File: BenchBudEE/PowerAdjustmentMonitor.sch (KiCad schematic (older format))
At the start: 0 parts

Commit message: Populated the Power Adjustment Monitor sheet in rough form.
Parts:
- added JP? (x3): JUMPER, ~, symbol JUMPER
- added R? (x8): R, ~, symbol R
- added R? (x2): RVAR, ~, symbol RVAR
- added U? (x2): LM317, ~, symbol LM317
- added U? (x2): 7805, ~, symbol 7805
- added U? (x2): LM324, symbol LM324
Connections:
- net labels added: +12V, +3.3V, +5V, -12V, 3V3_MON, 5V_MON, AGND, FE_V+, FE_V-, GND, V+_ADJ, V+_ADJ_MON, V+_CURR_MON, V+_MON, V-_ADJ, V-_ADJ_MON, V-_CURR_MON, V-_MON
- wire segments 0 -> 77
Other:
- note added: "Jumper to split the nets"
- note added: "Placeholder for now."
- note added: "Placeholder.\nRegulator TBD."

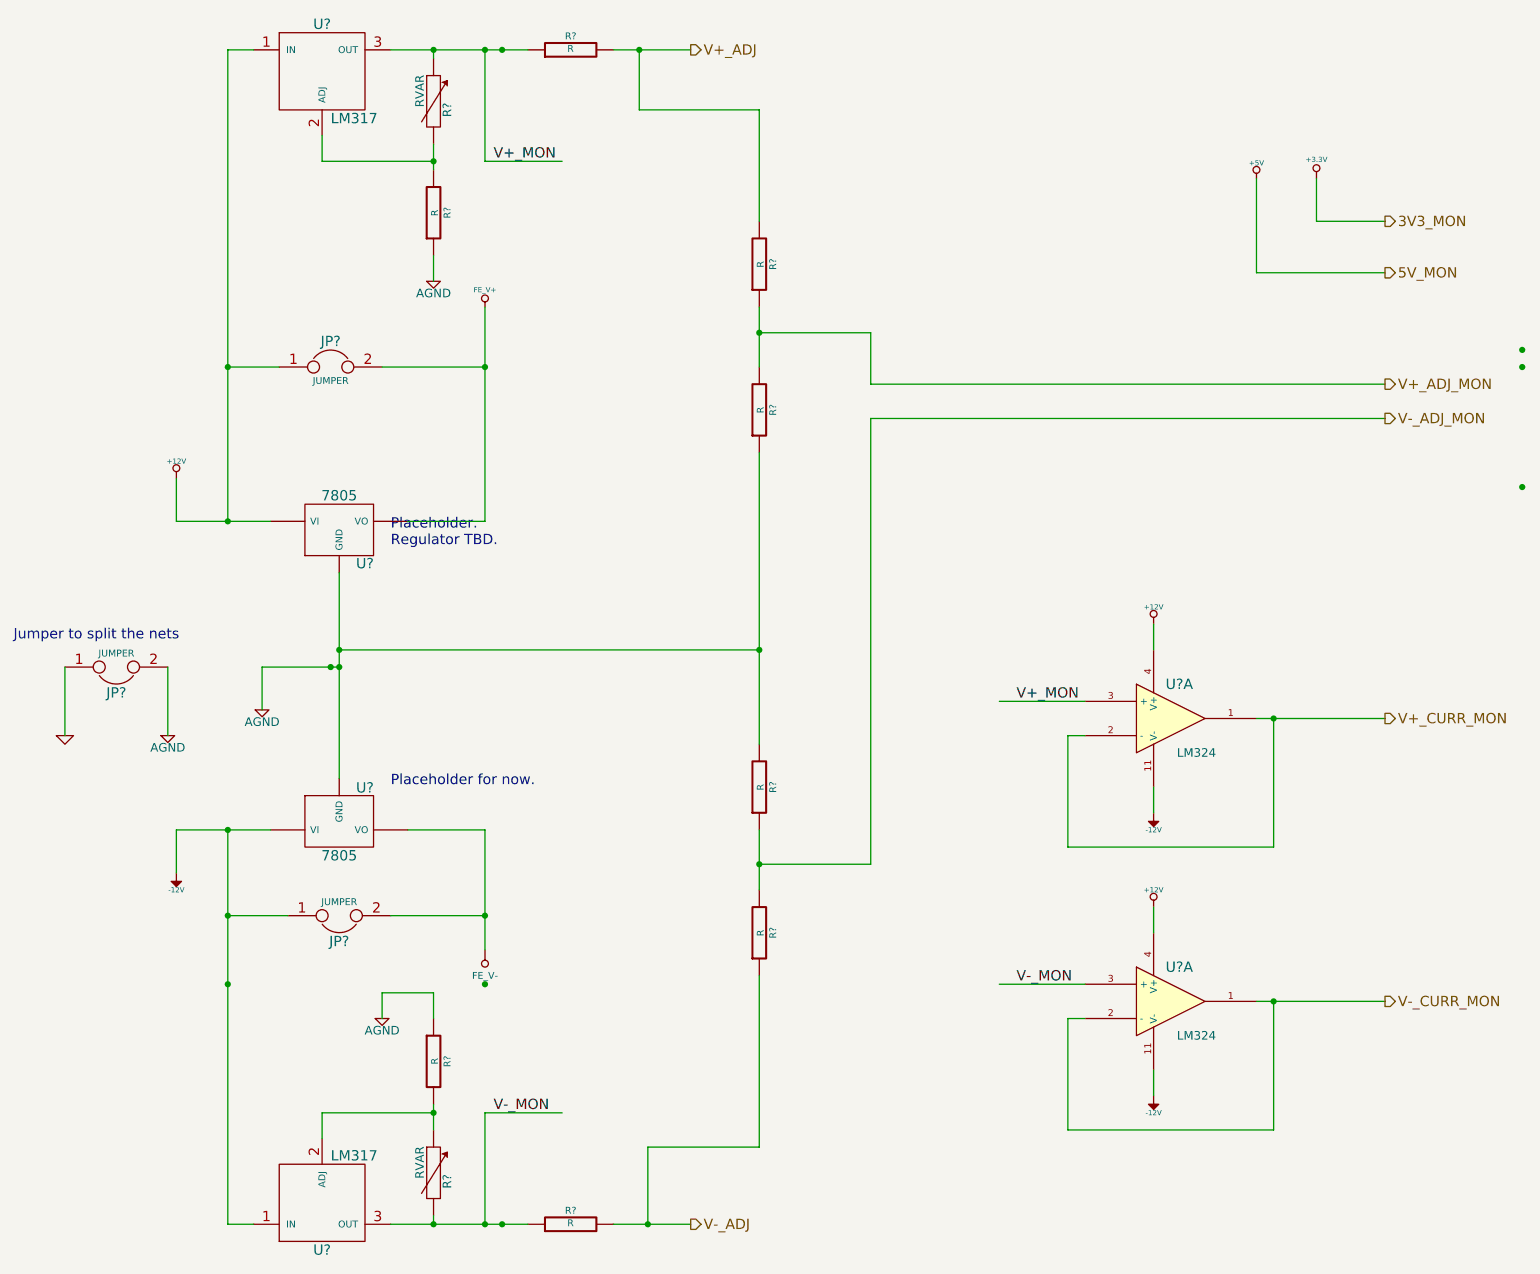
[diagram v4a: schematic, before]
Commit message: Connected Arduino power/ground. +5V power filtering. Removed current monitoring.
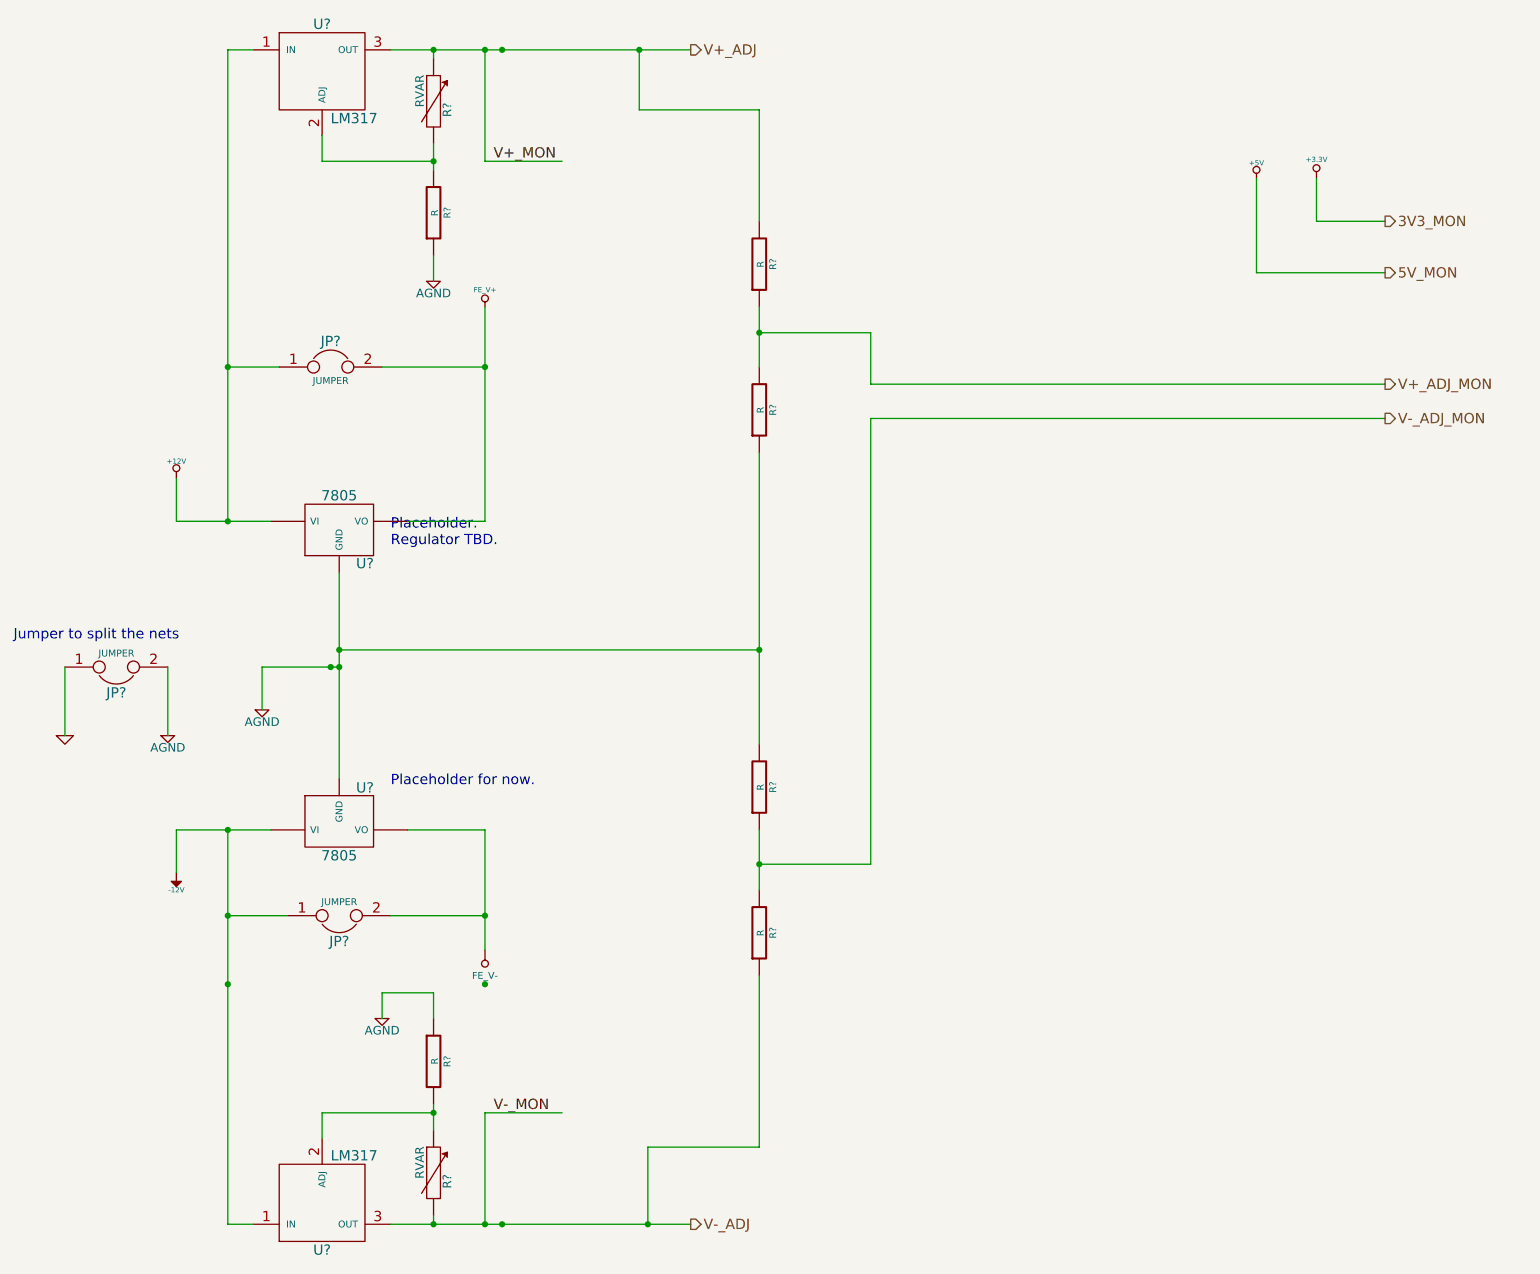
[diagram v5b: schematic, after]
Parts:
- removed R? (x2): R, ~, symbol R
- removed U? (x2): LM324, symbol LM324
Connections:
- net labels removed: V+_CURR_MON, V-_CURR_MON
- wire segments 77 -> 59
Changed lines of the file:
@@
 $Descr A4 11693 8268
 encoding utf-8
-Sheet 9 9
+Sheet 6 9
 Title ""
-Date "14 feb 2014"
+Date "19 feb 2014"
 Rev ""
 Comp ""
@@
 	1    0    0    1
 $EndComp
-Connection ~ 9300 2600
-Connection ~ 9300 2500
-Connection ~ 9300 3300
 Wire Wire Line
 	1450 5550 1450 5300
@@
 Connection ~ 1750 5800
 Wire Wire Line
-	2700 7600 3500 7600
+	2700 7600 4450 7600
 Wire Wire Line
 	2950 7600 2950 7550
@@
 Text HLabel 8500 2900 2    60   Output ~ 0
 V-_ADJ_MON
-Text HLabel 8500 6300 2    60   Output ~ 0
-V-_CURR_MON
-Text HLabel 8500 4650 2    60   Output ~ 0
-V+_CURR_MON
 $Comp
 L R R?
@@
 Wire Wire Line
 	7750 2050 7750 1500
-$Comp
-L R R?
-U 1 1 52F7546A
-P 3750 7600
-F 0 "R?" V 3830 7600 40  0000 C CNN
-F 1 "R" V 3757 7601 40  0000 C CNN
-F 2 "~" V 3680 7600 30  0000 C CNN
-F 3 "~" H 3750 7600 30  0000 C CNN
-	1    3750 7600
-	0    -1   -1   0
-$EndComp
-Wire Wire Line
-	4000 7600 4450 7600
 Wire Wire Line
 	4200 7600 4200 7150
@@
 	4200 7150 4850 7150
 Connection ~ 4200 7600
-$Comp
-L R R?
-U 1 1 52F7576B
-P 3750 750
-F 0 "R?" V 3830 750 40  0000 C CNN
-F 1 "R" V 3757 751 40  0000 C CNN
-F 2 "~" V 3680 750 30  0000 C CNN
-F 3 "~" H 3750 750 30  0000 C CNN
-	1    3750 750
-	0    -1   -1   0
-$EndComp
-Wire Wire Line
-	2700 750  3500 750
-Wire Wire Line
-	4000 750  4450 750
+Wire Wire Line
+	2700 750  4450 750
 Wire Wire Line
 	4850 1100 4150 1100
@@
 Text Label 3300 1400 0    60   ~ 0
 V+_MON
-$Comp
-L LM324 U?
-U 1 1 52F76215
-P 7250 6300
-F 0 "U?" H 7300 6500 60  0000 C CNN
-F 1 "LM324" H 7400 6100 50  0000 C CNN
-F 2 "" H 7250 6300 60  0000 C CNN
-F 3 "" H 7250 6300 60  0000 C CNN
-	1    7250 6300
-	1    0    0    -1
-$EndComp
-$Comp
-L +12V #PWR?
-U 1 1 52F76385
-P 7150 5750
-F 0 "#PWR?" H 7150 5700 20  0001 C CNN
-F 1 "+12V" H 7150 5850 30  0000 C CNN
-F 2 "" H 7150 5750 60  0000 C CNN
-F 3 "" H 7150 5750 60  0000 C CNN
-	1    7150 5750
-	1    0    0    -1
-$EndComp
-Wire Wire Line
-	7150 5750 7150 5900
-$Comp
-L -12V #PWR?
-U 1 1 52F763E4
-P 7150 6850
-F 0 "#PWR?" H 7150 6980 20  0001 C CNN
-F 1 "-12V" H 7150 6950 30  0000 C CNN
-F 2 "" H 7150 6850 60  0000 C CNN
-F 3 "" H 7150 6850 60  0000 C CNN
-	1    7150 6850
-	1    0    0    1
-$EndComp
-Wire Wire Line
-	7150 6850 7150 6700
 Wire Wire Line
 	4850 5500 5500 5500
@@
 	5500 2400 5500 2700
 $Comp
-L LM324 U?
-U 1 1 52F76762
-P 7250 4650
-F 0 "U?" H 7300 4850 60  0000 C CNN
-F 1 "LM324" H 7400 4450 50  0000 C CNN
-F 2 "" H 7250 4650 60  0000 C CNN
-F 3 "" H 7250 4650 60  0000 C CNN
-	1    7250 4650
-	1    0    0    -1
-$EndComp
-$Comp
-L +12V #PWR?
-U 1 1 52F76768
-P 7150 4100
-F 0 "#PWR?" H 7150 4050 20  0001 C CNN
-F 1 "+12V" H 7150 4200 30  0000 C CNN
-F 2 "" H 7150 4100 60  0000 C CNN
-F 3 "" H 7150 4100 60  0000 C CNN
-	1    7150 4100
-	1    0    0    -1
-$EndComp
-Wire Wire Line
-	7150 4100 7150 4250
-$Comp
-L -12V #PWR?
-U 1 1 52F7676F
-P 7150 5200
-F 0 "#PWR?" H 7150 5330 20  0001 C CNN
-F 1 "-12V" H 7150 5300 30  0000 C CNN
-F 2 "" H 7150 5200 60  0000 C CNN
-F 3 "" H 7150 5200 60  0000 C CNN
-	1    7150 5200
-	1    0    0    1
-$EndComp
-Wire Wire Line
-	7150 5200 7150 5050
-Wire Wire Line
-	8500 6300 7750 6300
-Wire Wire Line
-	8500 4650 7750 4650
-Wire Wire Line
-	6750 4750 6650 4750
-Wire Wire Line
-	6650 4750 6650 5400
-Wire Wire Line
-	6650 5400 7850 5400
-Wire Wire Line
-	7850 5400 7850 4650
-Connection ~ 7850 4650
-Wire Wire Line
-	6750 4550 6250 4550
-Text Label 6350 4550 0    60   ~ 0
-V+_MON
-Wire Wire Line
-	6750 6400 6650 6400
-Wire Wire Line
-	6650 6400 6650 7050
-Wire Wire Line
-	6650 7050 7850 7050
-Wire Wire Line
-	7850 7050 7850 6300
-Connection ~ 7850 6300
-Wire Wire Line
-	6750 6200 6250 6200
-Text Label 6350 6200 0    60   ~ 0
-V-_MON
-$Comp
 L RVAR R?

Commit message: Placed the relay components.
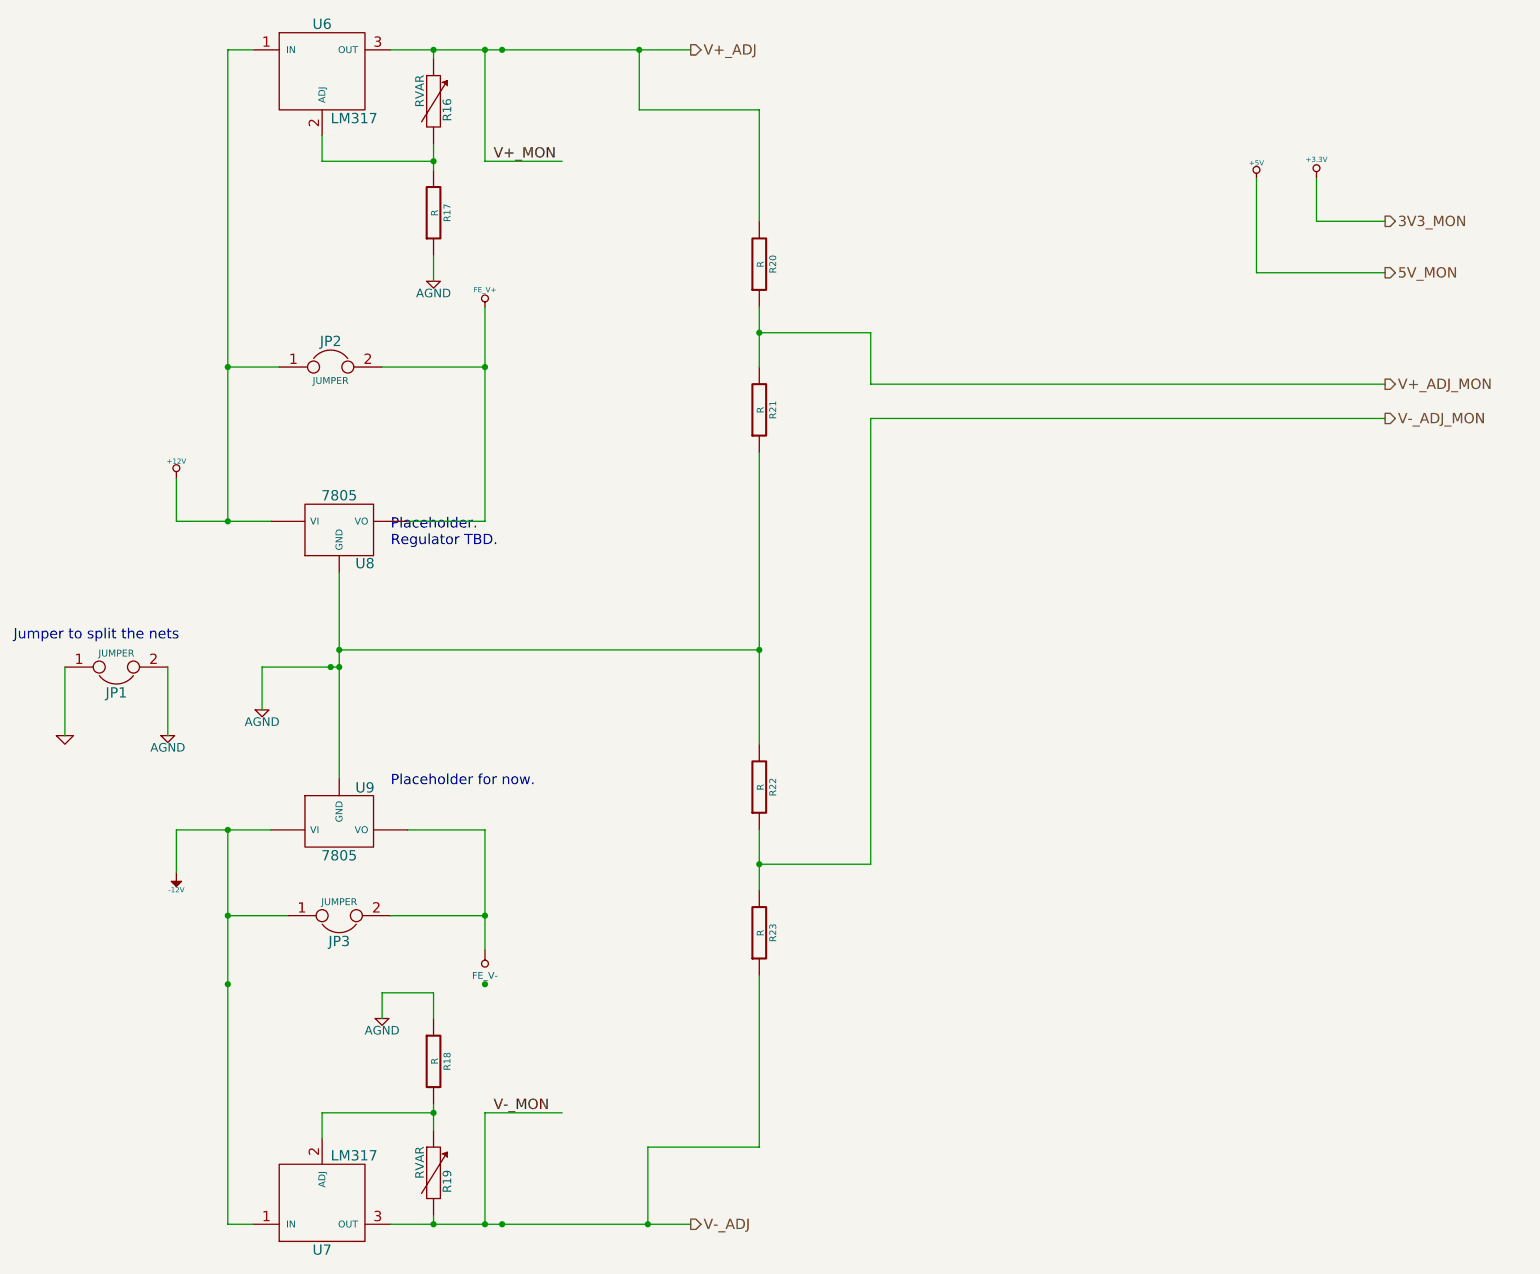
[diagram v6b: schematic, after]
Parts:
- gave numbers to parts that had none: 15
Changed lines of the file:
@@
 Sheet 6 9
 Title ""
-Date "19 feb 2014"
+Date "20 feb 2014"
 Rev ""
 Comp ""
@@
 $EndDescr
 $Comp
-L +12V #PWR?
+L +12V #PWR35
 U 1 1 52F6DADC
 P 1450 3250
-F 0 "#PWR?" H 1450 3200 20  0001 C CNN
+F 0 "#PWR35" H 1450 3200 20  0001 C CNN
 F 1 "+12V" H 1450 3350 30  0000 C CNN
 F 2 "" H 1450 3250 60  0000 C CNN
@@
 $EndComp
 $Comp
-L -12V #PWR?
+L -12V #PWR36
 U 1 1 52F6DAE4
 P 1450 5550
-F 0 "#PWR?" H 1450 5680 20  0001 C CNN
+F 0 "#PWR36" H 1450 5680 20  0001 C CNN
 F 1 "-12V" H 1450 5650 30  0000 C CNN
 F 2 "" H 1450 5550 60  0000 C CNN
@@
 $EndComp
 $Comp
-L +5V #PWR?
+L +5V #PWR42
 U 1 1 52F6DB6E
 P 7750 1500
-F 0 "#PWR?" H 7750 1590 20  0001 C CNN
+F 0 "#PWR42" H 7750 1590 20  0001 C CNN
 F 1 "+5V" H 7750 1590 30  0000 C CNN
 F 2 "" H 7750 1500 60  0000 C CNN
@@
 $EndComp
 $Comp
-L +3.3V #PWR?
+L +3.3V #PWR43
 U 1 1 52F6DB74
 P 8100 1500
-F 0 "#PWR?" H 8100 1460 30  0001 C CNN
+F 0 "#PWR43" H 8100 1460 30  0001 C CNN
 F 1 "+3.3V" H 8100 1610 30  0000 C CNN
 F 2 "" H 8100 1500 60  0000 C CNN
@@
 $EndComp
 $Comp
-L LM317 U?
+L LM317 U7
 U 1 1 52F71F0F
 P 2300 7450
-F 0 "U?" H 2300 7750 60  0000 C CNN
+F 0 "U7" H 2300 7750 60  0000 C CNN
 F 1 "LM317" H 2350 7200 60  0000 L CNN
 F 2 "~" H 2300 7450 60  0000 C CNN
@@
 Placeholder.\nRegulator TBD.
 $Comp
-L JUMPER JP?
+L JUMPER JP2
 U 1 1 52F720F4
 P 2350 2600
-F 0 "JP?" H 2350 2750 60  0000 C CNN
+F 0 "JP2" H 2350 2750 60  0000 C CNN
 F 1 "JUMPER" H 2350 2520 40  0000 C CNN
 F 2 "~" H 2350 2600 60  0000 C CNN
@@
 $EndComp
 $Comp
-L JUMPER JP?
+L JUMPER JP3
 U 1 1 52F72101
 P 2400 5800
-F 0 "JP?" H 2400 5950 60  0000 C CNN
+F 0 "JP3" H 2400 5950 60  0000 C CNN
 F 1 "JUMPER" H 2400 5720 40  0000 C CNN
 F 2 "~" H 2400 5800 60  0000 C CNN
@@
 $EndComp
 $Comp
-L GND #PWR?
+L GND #PWR33
 U 1 1 52F72349
 P 800 4750
-F 0 "#PWR?" H 800 4750 30  0001 C CNN
+F 0 "#PWR33" H 800 4750 30  0001 C CNN
 F 1 "GND" H 800 4680 30  0001 C CNN
 F 2 "" H 800 4750 60  0000 C CNN
@@
 $EndComp
 $Comp
-L AGND #PWR?
+L AGND #PWR34
 U 1 1 52F726D0
 P 1400 4750
-F 0 "#PWR?" H 1400 4750 40  0001 C CNN
+F 0 "#PWR34" H 1400 4750 40  0001 C CNN
 F 1 "AGND" H 1400 4680 50  0000 C CNN
 F 2 "" H 1400 4750 60  0000 C CNN
@@
 $EndComp
 $Comp
-L JUMPER JP?
+L JUMPER JP1
 U 1 1 52F726DD
 P 1100 4350
-F 0 "JP?" H 1100 4500 60  0000 C CNN
+F 0 "JP1" H 1100 4500 60  0000 C CNN
 F 1 "JUMPER" H 1100 4270 40  0000 C CNN
 F 2 "~" H 1100 4350 60  0000 C CNN
@@
 $EndComp
 $Comp
-L AGND #PWR?
+L AGND #PWR37
 U 1 1 52F72728
 P 1950 4600
-F 0 "#PWR?" H 1950 4600 40  0001 C CNN
+F 0 "#PWR37" H 1950 4600 40  0001 C CNN
 F 1 "AGND" H 1950 4530 50  0000 C CNN
 F 2 "" H 1950 4600 60  0000 C CNN
@@
 Jumper to split the nets
 $Comp
-L FE_V+ #PWR?
+L FE_V+ #PWR40
 U 1 1 52F72F13
 P 3250 2250
-F 0 "#PWR?" H 3250 2350 30  0001 C CNN
+F 0 "#PWR40" H 3250 2350 30  0001 C CNN
 F 1 "FE_V+" H 3250 2350 30  0000 C CNN
 F 2 "" H 3250 2250 60  0000 C CNN
@@
 $EndComp
 $Comp
-L FE_V- #PWR?
+L FE_V- #PWR41
 U 1 1 52F72F3C
 P 3250 6000
-F 0 "#PWR?" H 3250 6200 40  0001 C CNN
+F 0 "#PWR41" H 3250 6200 40  0001 C CNN
 F 1 "FE_V-" H 3250 6150 40  0000 C CNN
 F 2 "" H 3250 6000 60  0000 C CNN
@@
 $EndComp
 $Comp
-L 7805 U?
+L 7805 U8
 U 1 1 52F7316C
 P 2400 3550
-F 0 "U?" H 2550 3354 60  0000 C CNN
+F 0 "U8" H 2550 3354 60  0000 C CNN
 F 1 "7805" H 2400 3750 60  0000 C CNN
 F 2 "~" H 2400 3550 60  0000 C CNN
@@
 $EndComp
 $Comp
-L 7805 U?
+L 7805 U9
 U 1 1 52F73183
 P 2400 5250
-F 0 "U?" H 2550 5054 60  0000 C CNN
+F 0 "U9" H 2550 5054 60  0000 C CNN
 F 1 "7805" H 2400 5450 60  0000 C CNN
 F 2 "~" H 2400 5250 60  0000 C CNN
@@
 	2950 7600 2950 7550
 $Comp
-L R R?
+L R R18
 U 1 1 52F737B3
 P 2950 6650
-F 0 "R?" V 3030 6650 40  0000 C CNN
+F 0 "R18" V 3030 6650 40  0000 C CNN
 F 1 "R" V 2957 6651 40  0000 C CNN
 F 2 "~" V 2880 6650 30  0000 C CNN
@@
 	2650 6250 2650 6400
 $Comp
-L AGND #PWR?
+L AGND #PWR38
 U 1 1 52F7382B
 P 2650 6400
-F 0 "#PWR?" H 2650 6400 40  0001 C CNN
+F 0 "#PWR38" H 2650 6400 40  0001 C CNN
 F 1 "AGND" H 2650 6330 50  0000 C CNN
 F 2 "" H 2650 6400 60  0000 C CNN
@@
 Connection ~ 2950 7600
 $Comp
-L LM317 U?
+L LM317 U6
 U 1 1 52F73C8A
 P 2300 900
-F 0 "U?" H 2300 1200 60  0000 C CNN
+F 0 "U6" H 2300 1200 60  0000 C CNN
 F 1 "LM317" H 2350 650 60  0000 L CNN
 F 2 "~" H 2300 900 60  0000 C CNN
@@
 	2950 750  2950 800
 $Comp
-L R R?
+L R R17
 U 1 1 52F73C9A
 P 2950 1700
-F 0 "R?" V 3030 1700 40  0000 C CNN
+F 0 "R17" V 3030 1700 40  0000 C CNN
 F 1 "R" V 2957 1701 40  0000 C CNN
 F 2 "~" V 2880 1700 30  0000 C CNN
@@
 Connection ~ 2950 1400
 $Comp
-L AGND #PWR?
+L AGND #PWR39
 U 1 1 52F73CA7
 P 2950 2100
-F 0 "#PWR?" H 2950 2100 40  0001 C CNN
+F 0 "#PWR39" H 2950 2100 40  0001 C CNN
 F 1 "AGND" H 2950 2030 50  0000 C CNN
 F 2 "" H 2950 2100 60  0000 C CNN
@@
 V-_ADJ_MON
 $Comp
-L R R?
+L R R20
 U 1 1 52F74858
 P 4850 2000
-F 0 "R?" V 4930 2000 40  0000 C CNN
+F 0 "R20" V 4930 2000 40  0000 C CNN
 F 1 "R" V 4857 2001 40  0000 C CNN
 F 2 "~" V 4780 2000 30  0000 C CNN
@@
 $EndComp
 $Comp
-L R R?
+L R R21
 U 1 1 52F7485E
 P 4850 2850
-F 0 "R?" V 4930 2850 40  0000 C CNN
+F 0 "R21" V 4930 2850 40  0000 C CNN
 F 1 "R" V 4857 2851 40  0000 C CNN
 F 2 "~" V 4780 2850 30  0000 C CNN
@@
 	2400 3800 2400 5000
 $Comp
-L R R?
+L R R22
 U 1 1 52F74BD2
 P 4850 5050
-F 0 "R?" V 4930 5050 40  0000 C CNN
+F 0 "R22" V 4930 5050 40  0000 C CNN
 F 1 "R" V 4857 5051 40  0000 C CNN
 F 2 "~" V 4780 5050 30  0000 C CNN
@@
 $EndComp
 $Comp
-L R R?
+L R R23
 U 1 1 52F74BD8
 P 4850 5900
-F 0 "R?" V 4930 5900 40  0000 C CNN
+F 0 "R23" V 4930 5900 40  0000 C CNN
 F 1 "R" V 4857 5901 40  0000 C CNN
 F 2 "~" V 4780 5900 30  0000 C CNN
@@
 	5500 2400 5500 2700
 $Comp
-L RVAR R?
+L RVAR R19
 U 1 1 52F76E94
 P 2950 7300
-F 0 "R?" V 3030 7250 50  0000 C CNN
+F 0 "R19" V 3030 7250 50  0000 C CNN
 F 1 "RVAR" V 2870 7360 50  0000 C CNN
 F 2 "~" H 2950 7300 60  0000 C CNN
@@
 $EndComp
 $Comp
-L RVAR R?
+L RVAR R16
 U 1 1 52F76EA7
 P 2950 1050
-F 0 "R?" V 3030 1000 50  0000 C CNN
+F 0 "R16" V 3030 1000 50  0000 C CNN
 F 1 "RVAR" V 2870 1110 50  0000 C CNN
 F 2 "~" H 2950 1050 60  0000 C CNN
